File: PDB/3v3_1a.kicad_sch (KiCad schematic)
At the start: 13 parts, among them U12 TLV62569ADRLR, U13 INA228

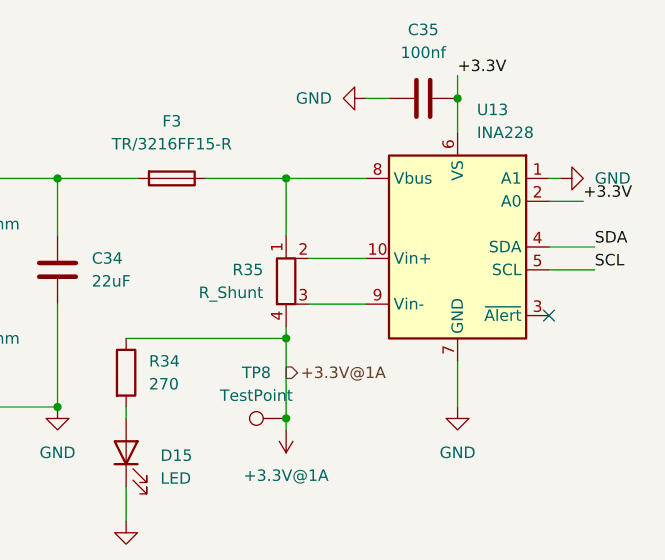
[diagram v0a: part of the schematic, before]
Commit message: last push before removing oring
i think we're going with an interlock system instead. the battery oring on here will take far too much physical room on the board to make it worthwhile. this push removes the oring and assumes a single power input.
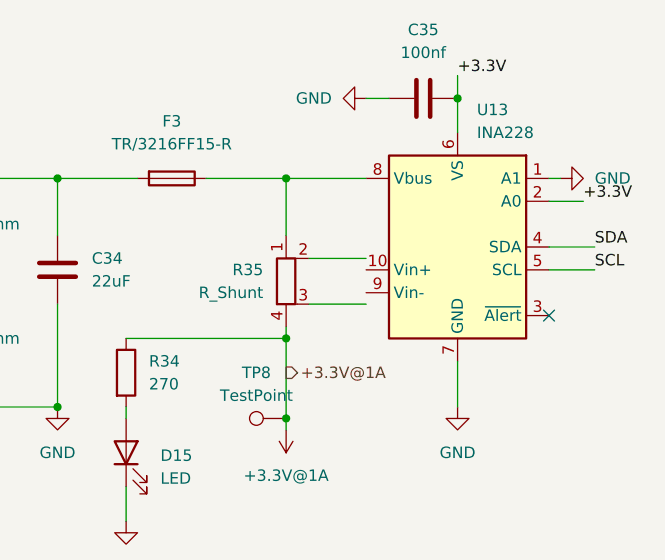
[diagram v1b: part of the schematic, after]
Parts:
- U12: footprint Dependencies:TLV62569ADRLR -> DRL0006A
- U13: footprint Package_SO:HVSSOP-10-1EP_3x3mm_P0.5mm_EP1.83x1.89mm -> Package_SO:TSSOP-10_3x3mm_P0.5mm
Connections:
- net at R35.2: no longer U13.10 (Vin+)
- net at R35.3: no longer U13.9 (Vin-)
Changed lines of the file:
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@@
 			)
 		)
-		(property "Footprint" "Dependencies:TLV62569ADRLR"
+		(property "Footprint" "DRL0006A"
 			(at 58.42 67.31 0)
 			(hide yes)
@@
 			)
 		)
-		(property "Footprint" "Package_SO:HVSSOP-10-1EP_3x3mm_P0.5mm_EP1.83x1.89mm"
+		(property "Footprint" "Package_SO:TSSOP-10_3x3mm_P0.5mm"
 			(at 179.832 44.704 0)
 			(hide yes)

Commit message: did lots of routing
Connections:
- net +3.3V@1A is gone; now on net +3.3V: R34.1, R35.4, TP8.1
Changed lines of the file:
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@@
 			)
 		)
-		(property "Value" "+3.3V@1A"
-			(at 135.89 92.71 0)
+		(property "Value" "+3.3V"
+			(at 138.43 88.8999 0)
 			(show_name no)
 			(do_not_autoplace no)
@@
 					(size 1.27 1.27)
 				)
+				(justify right)
 			)
 		)
